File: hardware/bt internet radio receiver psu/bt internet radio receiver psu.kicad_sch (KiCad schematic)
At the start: 42 parts, among them J1 Screw_Terminal_01x03, J3 ±15V, J5 ±5V, J7 +5V_isolated, J8 VU_meter_pwr, J9 Screw_Terminal_01x02, Q1 PN2222A, Q2 PN2222A, U1 LM7815_TO220, U2 LM7915_TO220, U3 LM7805_TO220, U4 LM7905_TO220, U5 DC_DC_small

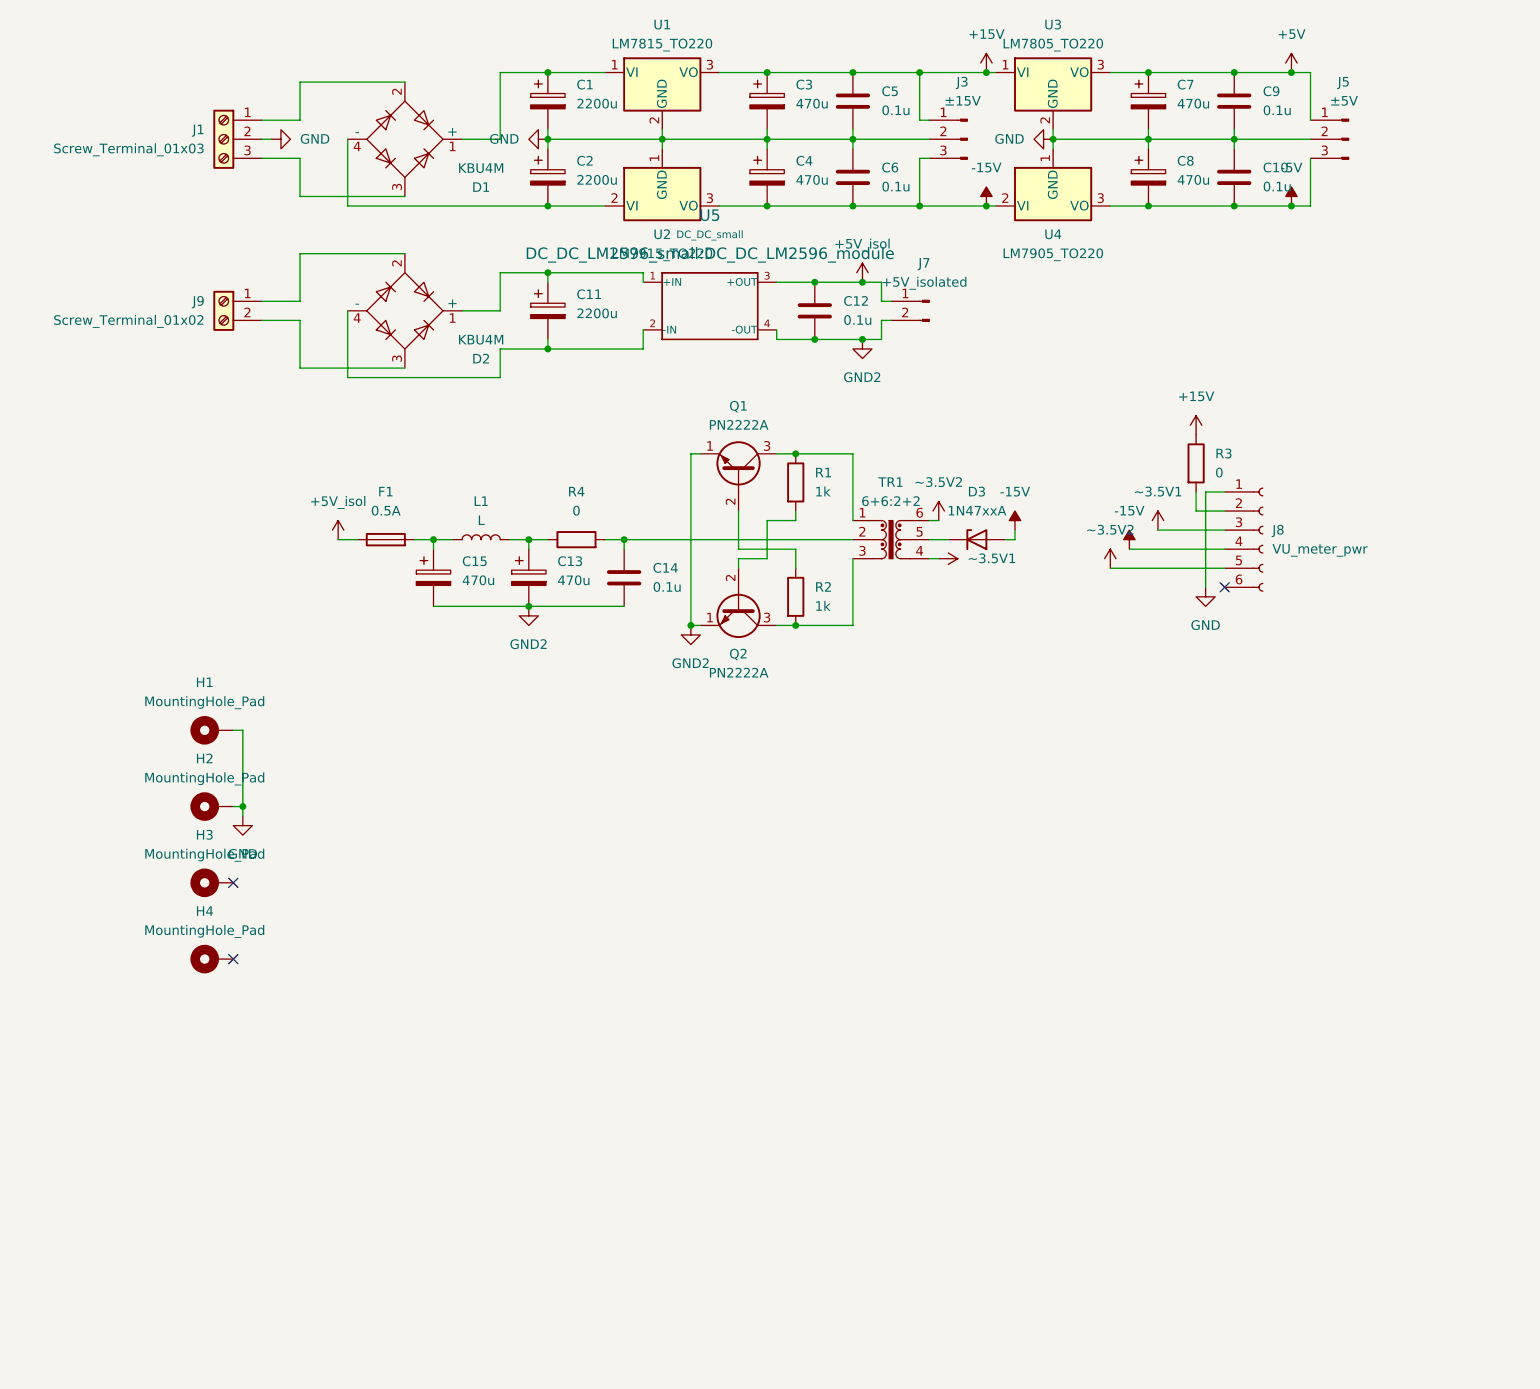
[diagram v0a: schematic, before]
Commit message: Cosmetic cleanup in schematics, add schematic PDF exports
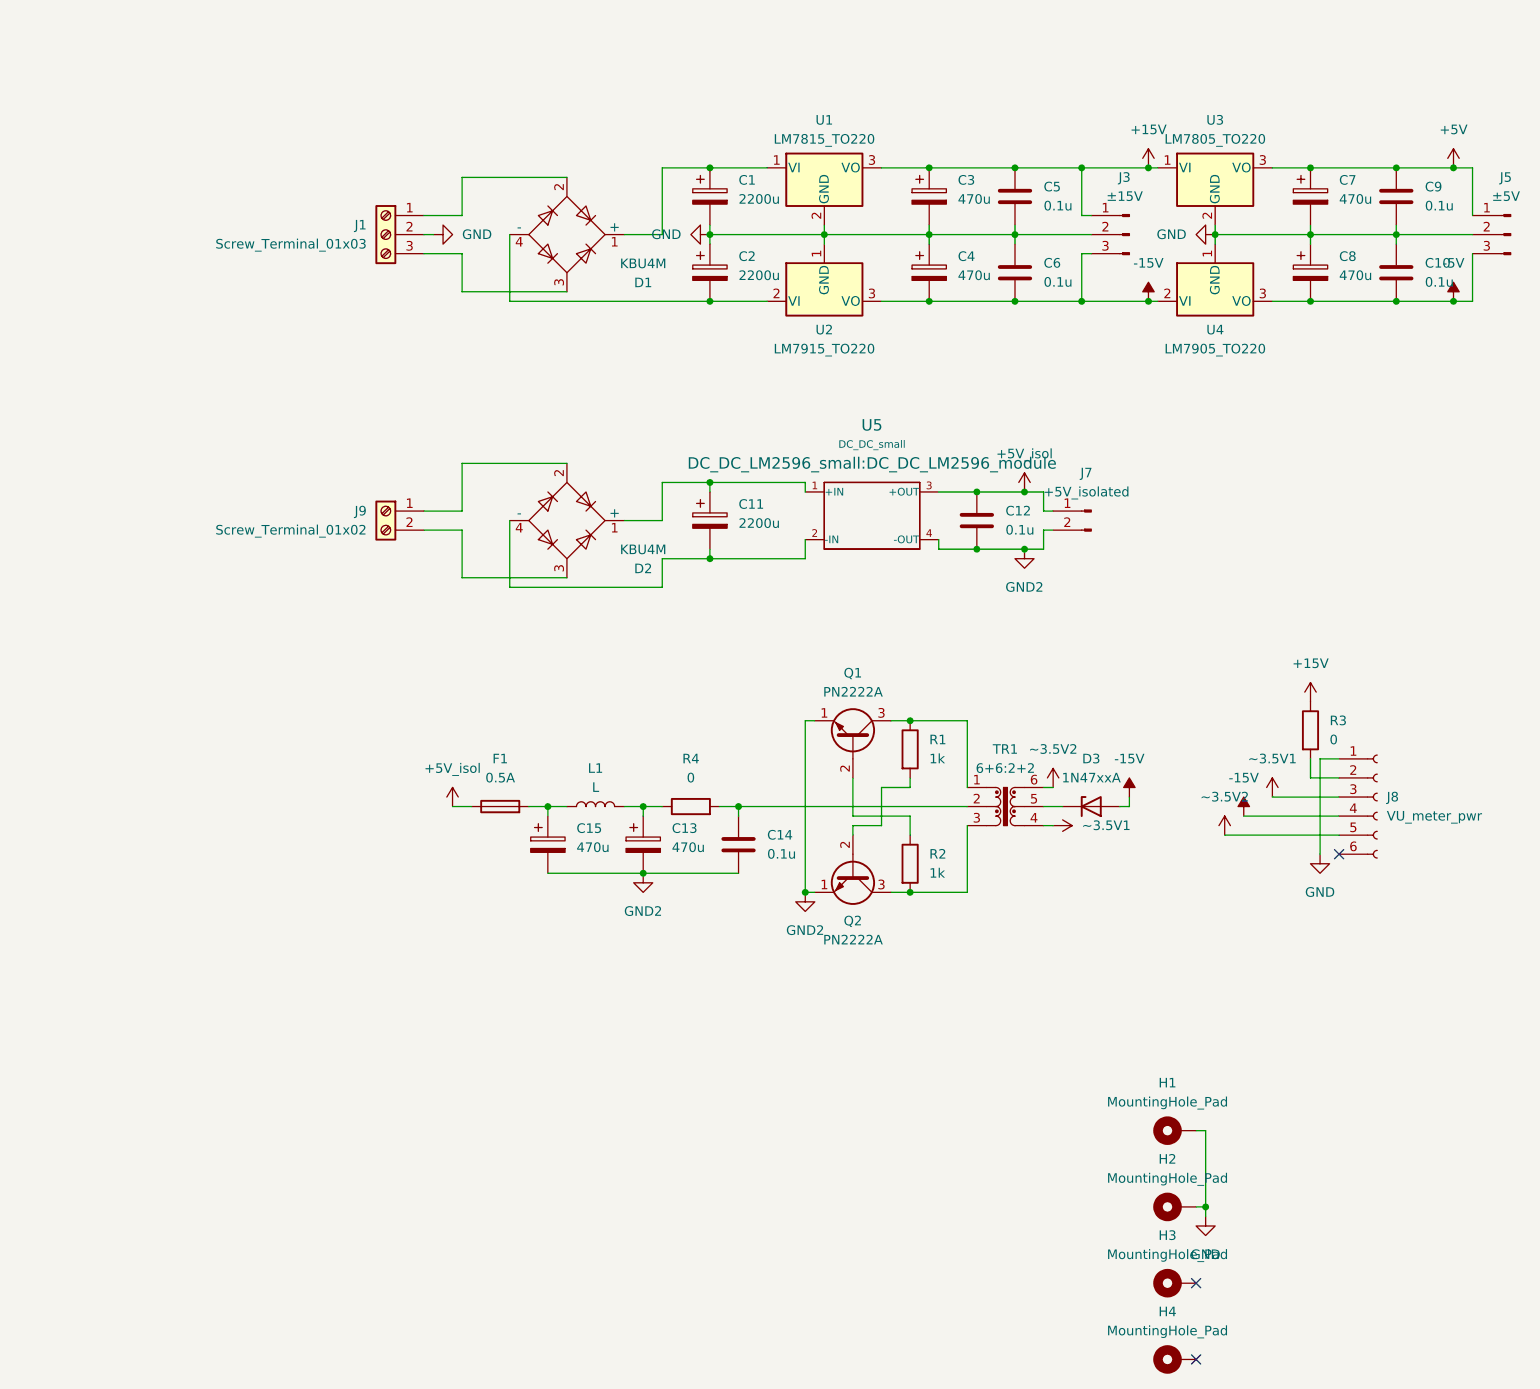
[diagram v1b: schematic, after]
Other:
- title: (none) -> Audiostreamer PSU
- moved on the sheet: C1, C10, C11, C12, C13, C14, C15, C2, C3, C4, C5, C6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
